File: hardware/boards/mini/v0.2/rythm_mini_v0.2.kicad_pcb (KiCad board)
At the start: 8 copper layers, 20 x 45 mm, 90 parts, among them IC1 NAU88C22YG, IC3 IS42S16160J-6BLI, J1 Bottom, J3 Top, Q1 PMV37EN22, U1 W25Q128JVP, U2 LTV-217-G, U4 STM32H750XBHx, Y1 Crystal_GND24

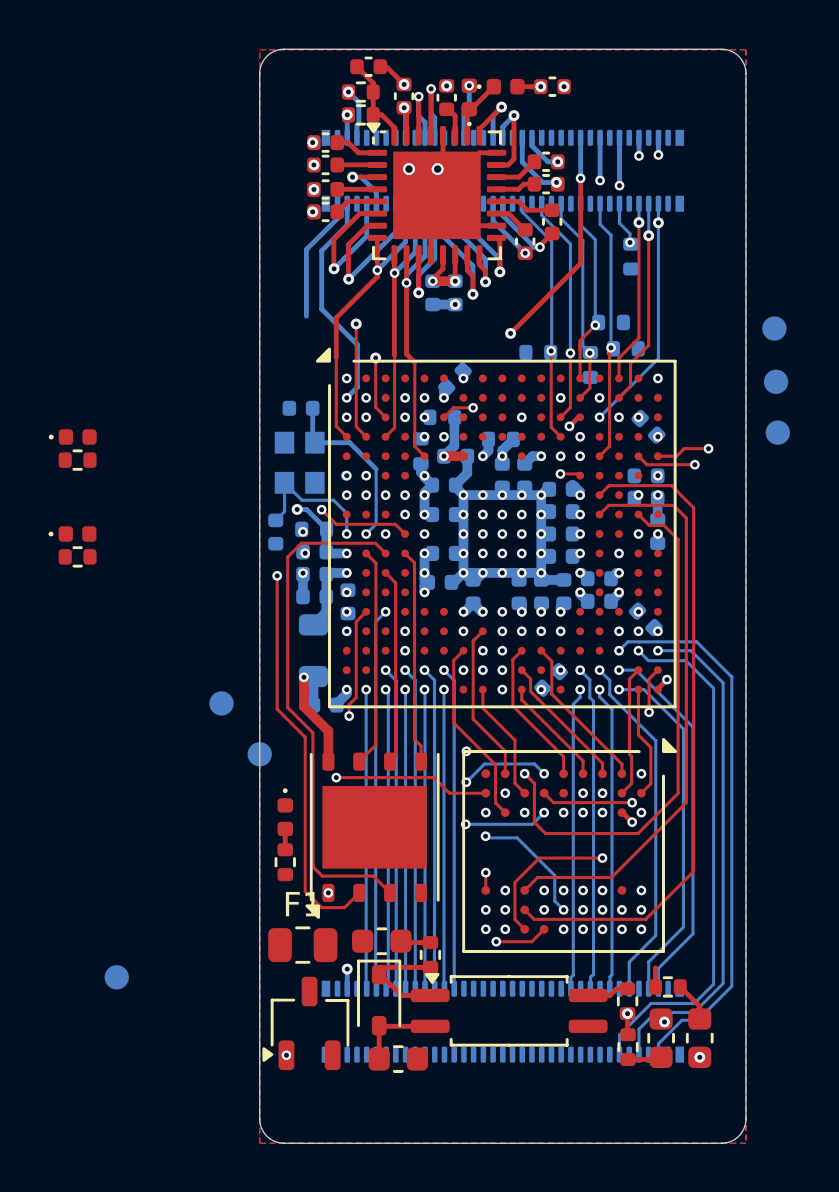
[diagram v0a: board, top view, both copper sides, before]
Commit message: mini: add SDRAM decoupling
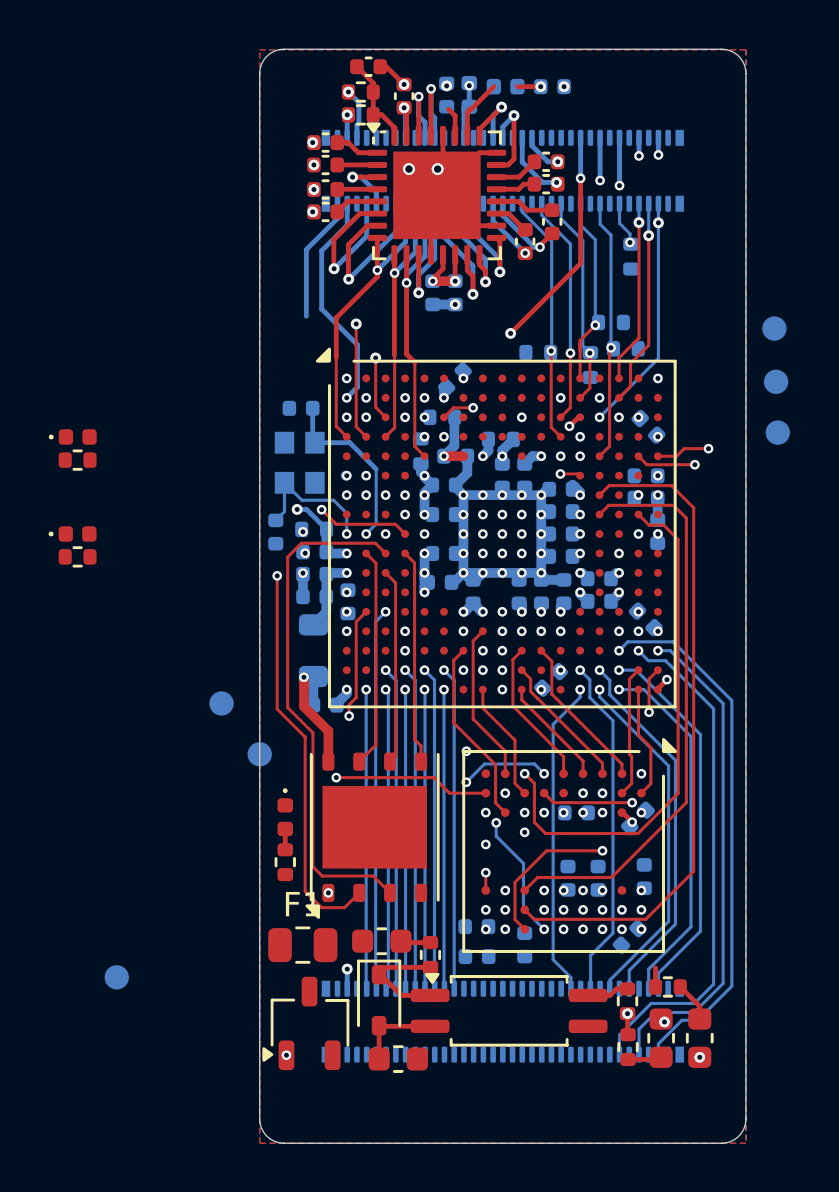
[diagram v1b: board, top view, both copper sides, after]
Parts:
- added C10: 100nF, Capacitor_SMD:C_0402_1005Metric, B.Cu at (85.6, 86.6)
- added C11: 100nF, Capacitor_SMD:C_0402_1005Metric, B.Cu at (85.8, 89.0)
- added C12: 100nF, Capacitor_SMD:C_0402_1005Metric, B.Cu at (83.9, 89.1)
- added C13: 100nF, Capacitor_SMD:C_0402_1005Metric, B.Cu at (85.2, 91.5)
- added C14: 100nF, Capacitor_SMD:C_0402_1005Metric, B.Cu at (82.7, 89.1)
- added C34: 10uF, Capacitor_SMD:C_0402_1005Metric, B.Cu at (78.9, 92.3)
- added C35: 10uF, Capacitor_SMD:C_0402_1005Metric, B.Cu at (80.9, 91.8)
- added C8: 100nF, Capacitor_SMD:C_0402_1005Metric, B.Cu at (83.0, 86.4)
- added C9: 100nF, Capacitor_SMD:C_0402_1005Metric, B.Cu at (78.9, 91.1)
- C18, C29, D5, D6: moved to B.Cu
- moved C29 0.11 mm to (77.7, 56.9)
- moved D6 0.10 mm to (78.6, 56.9)
- turned C18 to 180 degrees
- turned D5 to 180 degrees
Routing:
- net /PB13: track 12.6 -> 14.5 mm
- net /FMC_SDNWE: track 16.5 -> 14.6 mm, vias 2 -> 3
- net GND: track 39.2 -> 40.2 mm
- net +3.3V: track 45.4 -> 44.4 mm
- net /PB12: track 14.5 -> 15.2 mm
- net /PH8: track 13.4 -> 14.0 mm
- net /PH7: track 12.5 -> 13.1 mm
- net /PD11: track 22.6 -> 22.0 mm

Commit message: mini: downsized mezzanine from 70 pin to 60
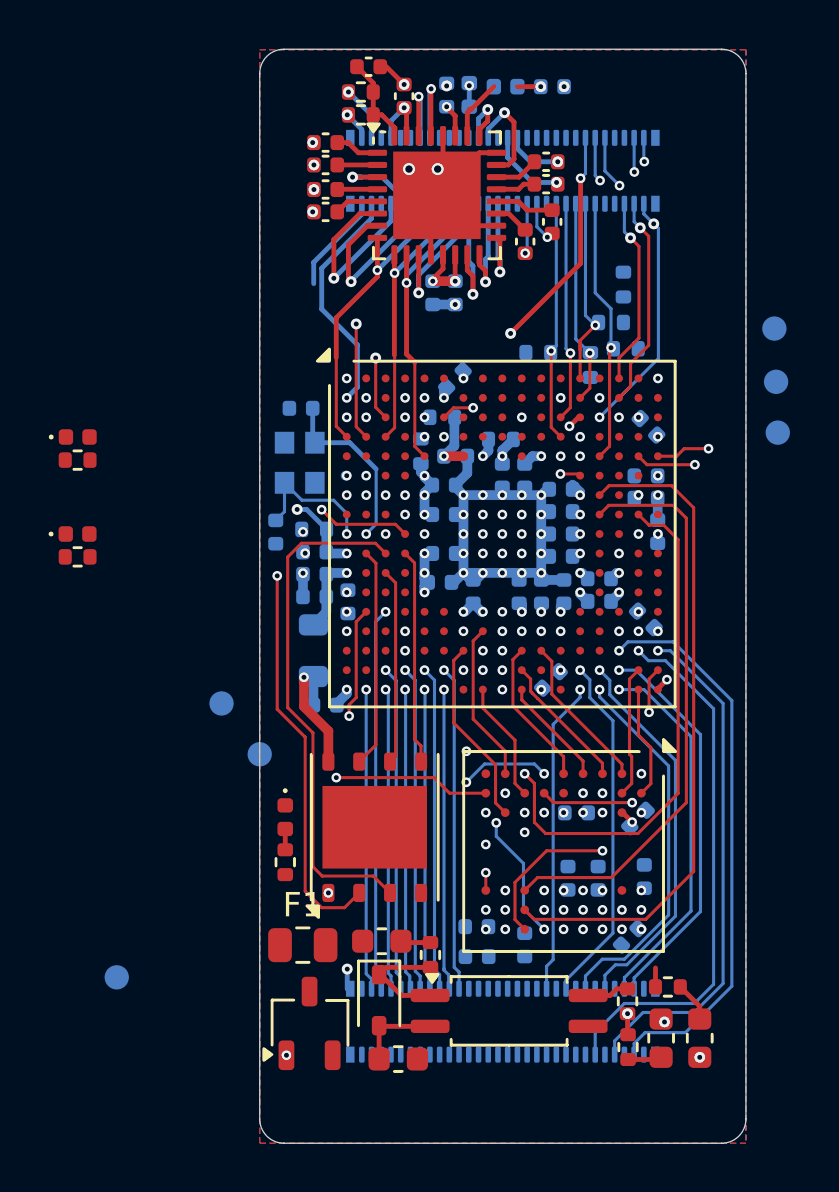
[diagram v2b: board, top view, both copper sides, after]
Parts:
- removed J1: Bottom, Connector_Hirose_DF40:Hirose_DF40C-70DP-0.4V_2x35-1MP_P0.4mm
- added J2: Top, Connector_Hirose_DF40:Hirose_DF40C-60DP-0.4V_2x30-1MP_P0.4mm, B.Cu at (80.0, 60.0)
- J3: value Top -> Bottom; footprint Connector_Hirose_DF40:Hirose_DF40C-70DP-0.4V_2x35-1MP_P0.4mm -> Connector_Hirose_DF40:Hirose_DF40C-60DP-0.4V_2x30-1MP_P0.4mm
- moved J3 35.0 mm to (80.0, 95.0)
- moved R11 1.19 mm to (85.0, 64.7)
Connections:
- J3 pad 11: /SWD_IO -> unconnected-(J3-Pad11)
- J3 pad 12: /SDMMC1_D0 -> /PD12
- J3 pad 13: unconnected-(J3-Pad13) -> /PB13
- J3 pad 15: /SWD_CLK -> unconnected-(J3-Pad15)
- J3 pad 16: /SDMMC1_D1 -> unconnected-(J3-Pad16)
- J3 pad 17: unconnected-(J3-Pad17) -> /PH8
- J3 pad 19: /SWD_SWO -> unconnected-(J3-Pad19)
- J3 pad 20: /SDMMC1_D2 -> unconnected-(J3-Pad20)
- J3 pad 21: unconnected-(J3-Pad21) -> /PH7
- J3 pad 24: /SDMMC1_D3 -> unconnected-(J3-Pad24)
- J3 pad 25: unconnected-(J3-Pad25) -> /DIN_OUT_SINK
- J3 pad 27: unconnected-(J3-Pad27) -> /DIN_OUT_SOURCE
- J3 pad 28: /SDMMC1_CK -> unconnected-(J3-Pad28)
- J3 pad 29: /AUX_OUT_L -> unconnected-(J3-Pad29)
- J3 pad 3: /PA11/4RX -> /USB_D+
- J3 pad 31: /AUX_OUT_R -> /DIN_IN_SOURCE
- J3 pad 32: /SDMMC1_CMD -> unconnected-(J3-Pad32)
- J3 pad 33: unconnected-(J3-Pad33) -> /DIN_IN_SINK
- J3 pad 35: /SPKR -> unconnected-(J3-Pad35)
- J3 pad 36: /AUX_IN_R -> unconnected-(J3-Pad36)
- J3 pad 37: /SPKL -> unconnected-(J3-Pad37)
- J3 pad 38: /AUX_IN_L -> unconnected-(J3-Pad38)
- J3 pad 39: unconnected-(J3-Pad39) -> /PJ2
- J3 pad 4: /SPI_MOSI -> /PD11
- J3 pad 41: unconnected-(J3-Pad41) -> /PJ3
- J3 pad 42: /I2C_SDA -> unconnected-(J3-Pad42)
- J3 pad 43: /VDDSPK -> /PB1
- J3 pad 44: /I2C_SCL -> unconnected-(J3-Pad44)
- J3 pad 45: unconnected-(J3-Pad45) -> /PB0
- J3 pad 47: unconnected-(J3-Pad47) -> /PC4
- J3 pad 48: /CODEC_GPIO -> unconnected-(J3-Pad48)
- J3 pad 49: /HPR -> /PC5
- J3 pad 5: unconnected-(J3-Pad5) -> /USB_D-
- J3 pad 50: /SAI1_MCLK -> unconnected-(J3-Pad50)
- J3 pad 51: /HPL -> /PA5
- J3 pad 52: /SAI1_SD_A -> unconnected-(J3-Pad52)
- J3 pad 53: unconnected-(J3-Pad53) -> /PA4
- J3 pad 54: /SAI1_SD_B -> unconnected-(J3-Pad54)
- J3 pad 55: +3.3V -> /PA2
- J3 pad 56: /SAI1_SCK -> unconnected-(J3-Pad56)
- J3 pad 57: unconnected-(J3-Pad57) -> /PA3
- J3 pad 58: /SAI1_FS -> /3v3+
- J3 pad 6: /SPI_MISO -> unconnected-(J3-Pad6)
- J3 pad 7: /PA12/4TX -> unconnected-(J3-Pad7)
- J3 pad 8: /SPI_SCK -> /PD13
- J3 pad 9: unconnected-(J3-Pad9) -> /PB12
- J3 pad MP: (no net) -> GND
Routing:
- net /SDMMC1_D0: track 11.8 -> 2.60 mm, vias 2 -> 1
- net /AUX_IN_R: track 3.22 -> 1.55 mm
- net /LIN: track 2.73 -> 4.00 mm
- net /VDDSPK: track 2.24 -> 1.02 mm
- net /RIN: track 6.67 -> 7.86 mm
- net /PD12: track 21.0 -> 22.0 mm
- net /RST: track 8.49 -> 7.44 mm
- net /PD11: track 22.0 -> 23.0 mm
- net /PB13: track 14.5 -> 15.4 mm
- net GND: track 40.2 -> 41.0 mm
- net /PA11/4RX: track 16.1 -> 16.8 mm
- net /PD13: track 20.4 -> 21.1 mm
- net /PB12: track 15.2 -> 15.9 mm
- net /AUX_OUT_L: track 1.66 -> 2.33 mm
- net /PA12/4TX: track 16.9 -> 17.4 mm
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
